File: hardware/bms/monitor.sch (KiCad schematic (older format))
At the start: 1 part

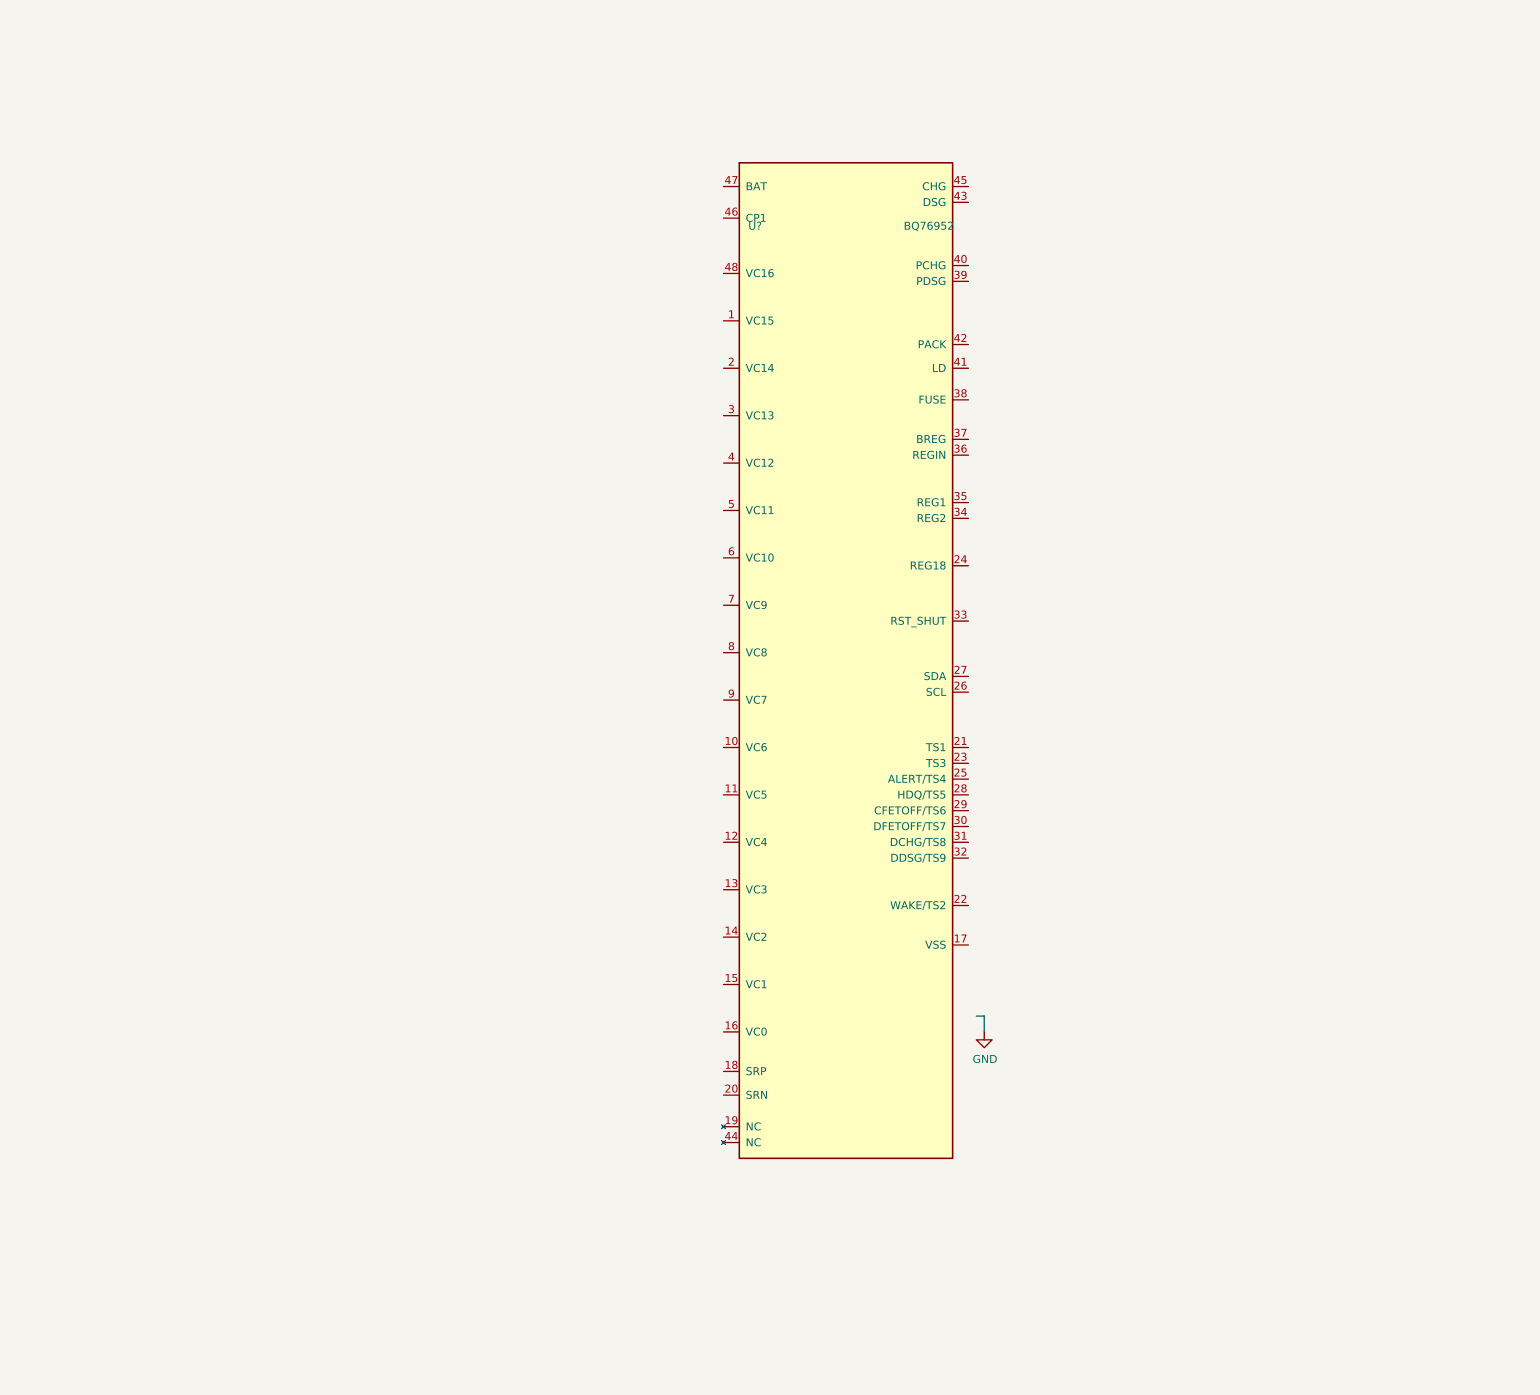
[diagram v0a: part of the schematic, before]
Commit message: More progress on battery management circuit
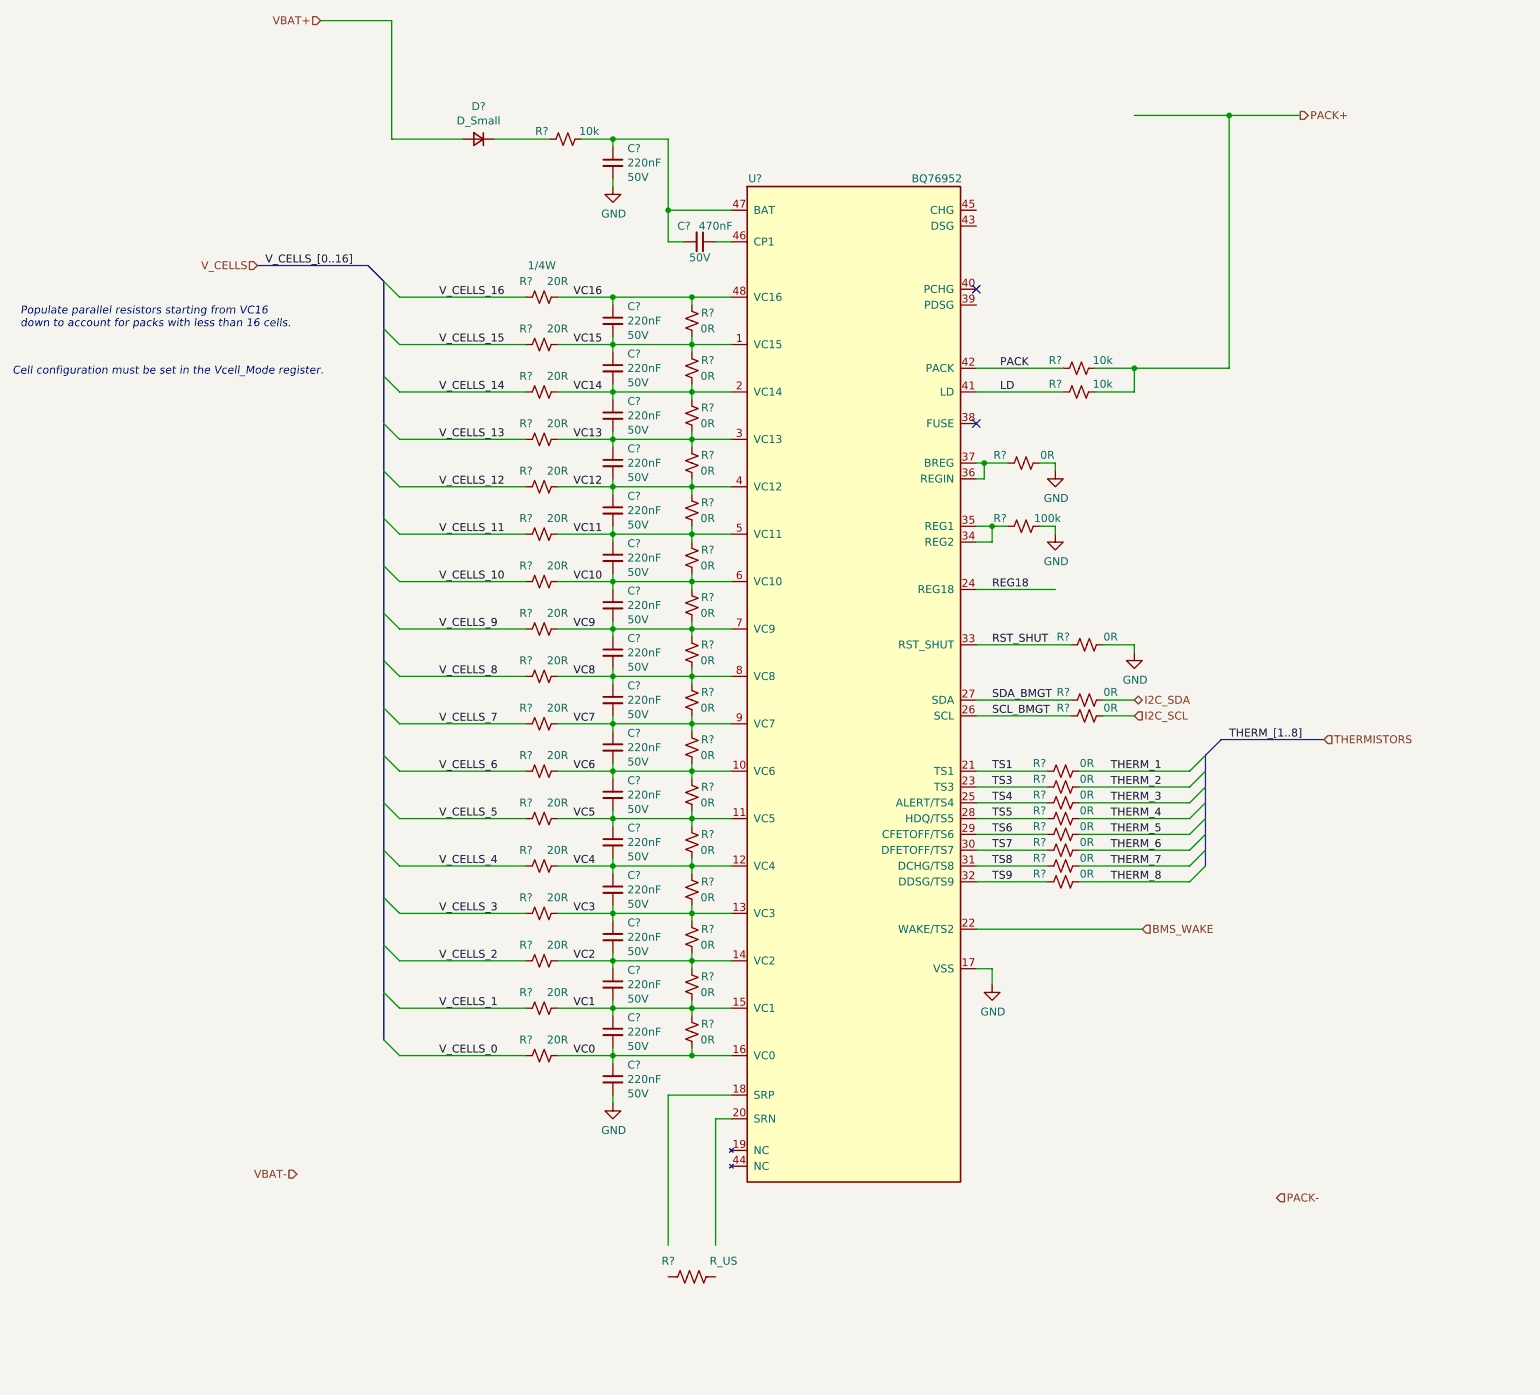
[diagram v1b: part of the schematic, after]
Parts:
- added C? (x18): 220nF, symbol Device:C_Small
- added C?: 470nF, symbol Device:C_Small
- added D?: D_Small, symbol Device:D_Small
- added R? (x17): 20R, symbol Device:R_Small_US
- added R? (x28): 0R, symbol Device:R_Small_US
- added R?: R_US, symbol Device:R_US
- added R?: 100k, symbol Device:R_Small_US
- added R? (x3): 10k, symbol Device:R_Small_US
- U?: MFG (none) -> Texas Instruments; MFG PN (none) -> BQ76952PFBR
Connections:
- net labels added: BMS_WAKE, I2C_SCL, I2C_SDA, LD, PACK, PACK+, PACK-, REG18, RST_SHUT, SCL_BMGT, SDA_BMGT, THERMISTORS, THERM_1, THERM_2, THERM_3, THERM_4, THERM_5, THERM_6, THERM_7, THERM_8, THERM_[1..8], TS1, TS3, TS4, TS5, TS6, TS7, TS8, TS9, VBAT+, VBAT-, VC0, VC1, VC10, VC11, VC12, VC13, VC14, VC15, VC16, VC2, VC3, VC4, VC5, VC6, VC7, VC8, VC9, V_CELLS, V_CELLS_0, V_CELLS_1, V_CELLS_10, V_CELLS_11, V_CELLS_12, V_CELLS_13, V_CELLS_14, V_CELLS_15, V_CELLS_16, V_CELLS_2, V_CELLS_3, V_CELLS_4, V_CELLS_5, V_CELLS_6, V_CELLS_7, V_CELLS_8, V_CELLS_9, V_CELLS_[0..16]
- wire segments 2 -> 199
- no-connect marks 0 -> 2
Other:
- note added: "Cell configuration must be set in the Vcell_Mode register.\n"
- note added: "Populate parallel resistors starting from VC16 \ndown to account for packs with less than 16 cells."
- moved on the sheet: U?
